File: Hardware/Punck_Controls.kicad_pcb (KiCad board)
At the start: 2 copper layers, 91.2 x 110 mm, 37 parts, among them J1 Conn_01x12_Female, J10 Kick_In, J11 USB_B_Micro, J12 Tempo_Out, J13 Audio_Out_L, J14 Audio_Out_R, J15 Midi_In, J2 Conn_01x12_Female, J3 Conn_01x12_Female, J4 Conn_01x12_Female, J5 Snare_In, J6 CH_In, J7 OH_In, J8 SamplerA_In, J9 SamplerB_In

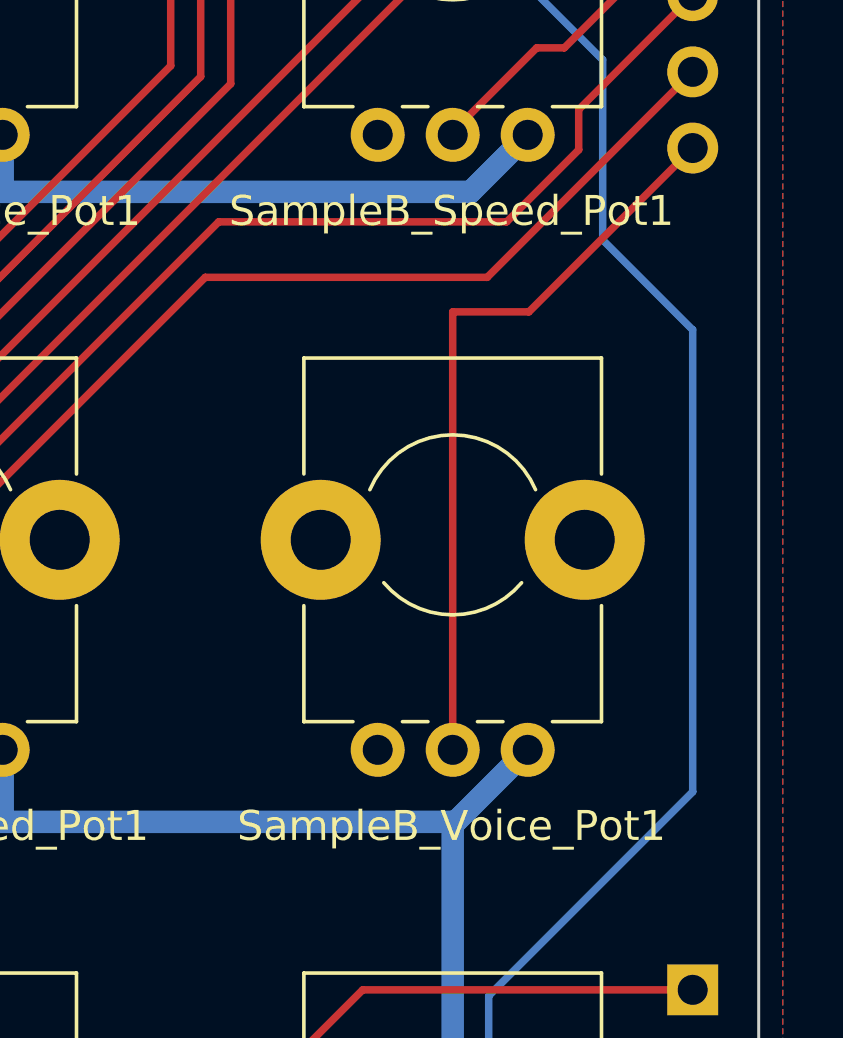
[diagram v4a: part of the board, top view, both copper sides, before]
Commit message: Updated components on panel board
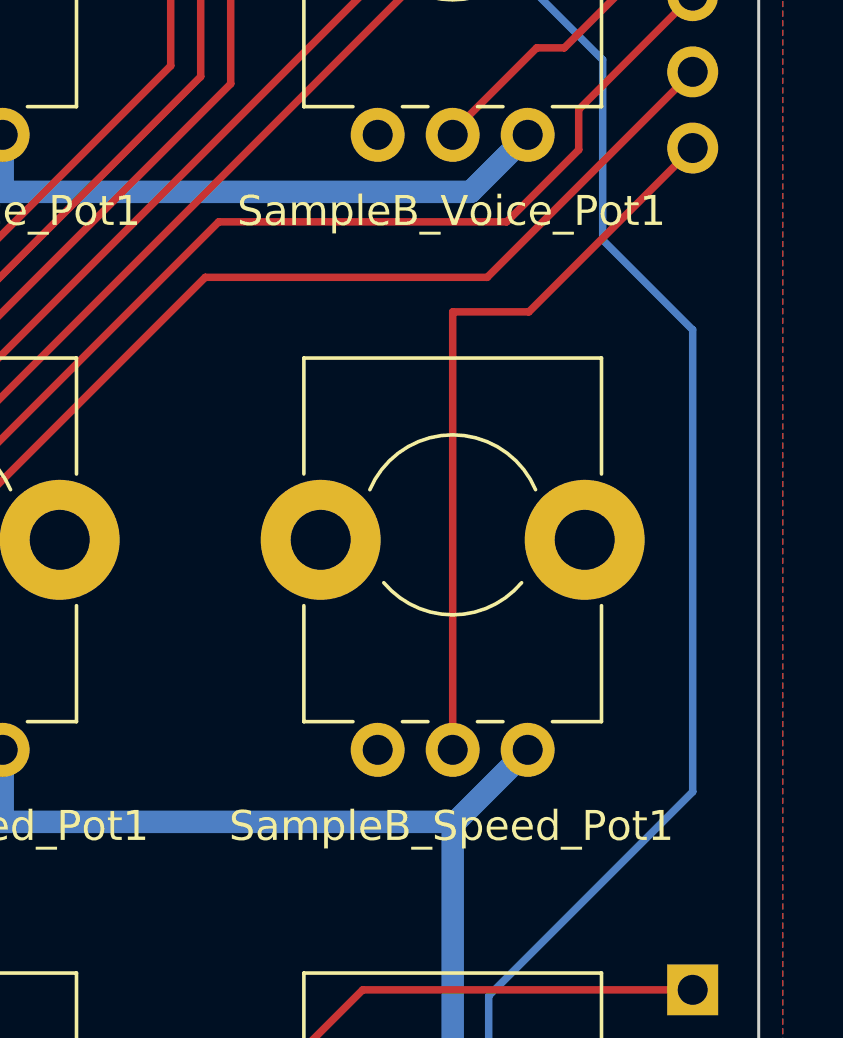
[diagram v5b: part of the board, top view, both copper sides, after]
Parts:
- moved SampleB_Speed_Pot1 20.5 mm to (151.0, 96.5)
- moved SampleB_Voice_Pot1 20.5 mm to (151.0, 76.0)
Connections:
- J1 pad 12: /SAMPLER_B_VOICE_POT -> /SAMPLER_B_SPEED_POT
- J1 pad 9: /SAMPLER_B_SPEED_POT -> /SAMPLER_B_VOICE_POT
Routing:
- net /SAMPLER_B_VOICE_POT: track 24.9 -> 11.0 mm
- net /SAMPLER_B_SPEED_POT: track 11.0 -> 24.9 mm
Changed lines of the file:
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@@
   )
   (footprint "Custom_Footprints:Alpha_9mm_Potentiometer_Aligned" (layer "F.Cu")
-    (at 151 76)
+    (at 151 96.5)
     (descr "Potentiometer 9mm")
     (tags "Potentiometer 9mm")
@@
   )
   (footprint "Custom_Footprints:Alpha_9mm_Potentiometer_Aligned" (layer "F.Cu")
-    (at 151 96.5)
+    (at 151 76)
     (descr "Potentiometer 9mm")
     (tags "Potentiometer 9mm")
@@
       (net 13 "/HIHAT_DECAY_POT") (pinfunction "Pin_8") (pintype "passive"))
     (pad "9" thru_hole oval (at 0 -20.32 180) (size 1.7 1.7) (drill 1) (layers *.Cu *.Mask)
-      (net 30 "/SAMPLER_B_SPEED_POT") (pinfunction "Pin_9") (pintype "passive"))
+      (net 26 "/SAMPLER_B_VOICE_POT") (pinfunction "Pin_9") (pintype "passive"))
     (pad "10" thru_hole oval (at 0 -22.86 180) (size 1.7 1.7) (drill 1) (layers *.Cu *.Mask)
       (net 32 "/SNARE_VOL_POT") (pinfunction "Pin_10") (pintype "passive"))
@@
       (net 29 "/SAMPLER_A_SPEED_POT") (pinfunction "Pin_11") (pintype "passive"))
     (pad "12" thru_hole oval (at 0 -27.94 180) (size 1.7 1.7) (drill 1) (layers *.Cu *.Mask)
-      (net 26 "/SAMPLER_B_VOICE_POT") (pinfunction "Pin_12") (pintype "passive"))
+      (net 30 "/SAMPLER_B_SPEED_POT") (pinfunction "Pin_12") (pintype "passive"))
     (model "${KICAD6_3DMODEL_DIR}/Connector_PinHeader_2.54mm.3dshapes/PinHeader_1x12_P2.54mm_Vertical.wrl"
       (offset (xyz 0 0 0))
@@
   (segment (start 141.7 63.6) (end 133.5 71.8) (width 0.25) (layer "F.Cu") (net 25))
   (segment (start 158.12 61.08) (end 155.6 63.6) (width 0.25) (layer "F.Cu") (net 25))
-  (segment (start 153.54 89.4) (end 159 83.94) (width 0.25) (layer "F.Cu") (net 26))
-  (segment (start 151 104) (end 151 89.4) (width 0.25) (layer "F.Cu") (net 26))
-  (segment (start 151 89.4) (end 153.54 89.4) (width 0.25) (layer "F.Cu") (net 26))
+  (segment (start 153.8 80.6) (end 154.72 80.6) (width 0.25) (layer "F.Cu") (net 26))
+  (segment (start 151 83.5) (end 151 83.4) (width 0.25) (layer "F.Cu") (net 26))
+  (segment (start 154.72 80.6) (end 159 76.32) (width 0.25) (layer "F.Cu") (net 26))
+  (segment (start 151 83.4) (end 153.8 80.6) (width 0.25) (layer "F.Cu") (net 26))
   (segment (start 154.26 114.54) (end 146.6 122.2) (width 0.25) (layer "F.Cu") (net 27))
   (segment (start 146.6 122.2) (end 135.8 122.2) (width 0.25) (layer "F.Cu") (net 27))
@@
   (segment (start 152.150489 88.249511) (end 159 81.4) (width 0.25) (layer "F.Cu") (net 29))
   (segment (start 133.5 97.5) (end 142.750489 88.249511) (width 0.25) (layer "F.Cu") (net 29))
-  (segment (start 153.8 80.6) (end 154.72 80.6) (width 0.25) (layer "F.Cu") (net 30))
-  (segment (start 151 83.5) (end 151 83.4) (width 0.25) (layer "F.Cu") (net 30))
-  (segment (start 154.72 80.6) (end 159 76.32) (width 0.25) (layer "F.Cu") (net 30))
-  (segment (start 151 83.4) (end 153.8 80.6) (width 0.25) (layer "F.Cu") (net 30))
+  (segment (start 153.54 89.4) (end 159 83.94) (width 0.25) (layer "F.Cu") (net 30))
+  (segment (start 151 104) (end 151 89.4) (width 0.25) (layer "F.Cu") (net 30))
+  (segment (start 151 89.4) (end 153.54 89.4) (width 0.25) (layer "F.Cu") (net 30))
   (segment (start 159 58.54) (end 154.74 62.8) (width 0.25) (layer "F.Cu") (net 31))
   (segment (start 119.6 81.4) (end 100.6 81.4) (width 0.25) (layer "F.Cu") (net 31))

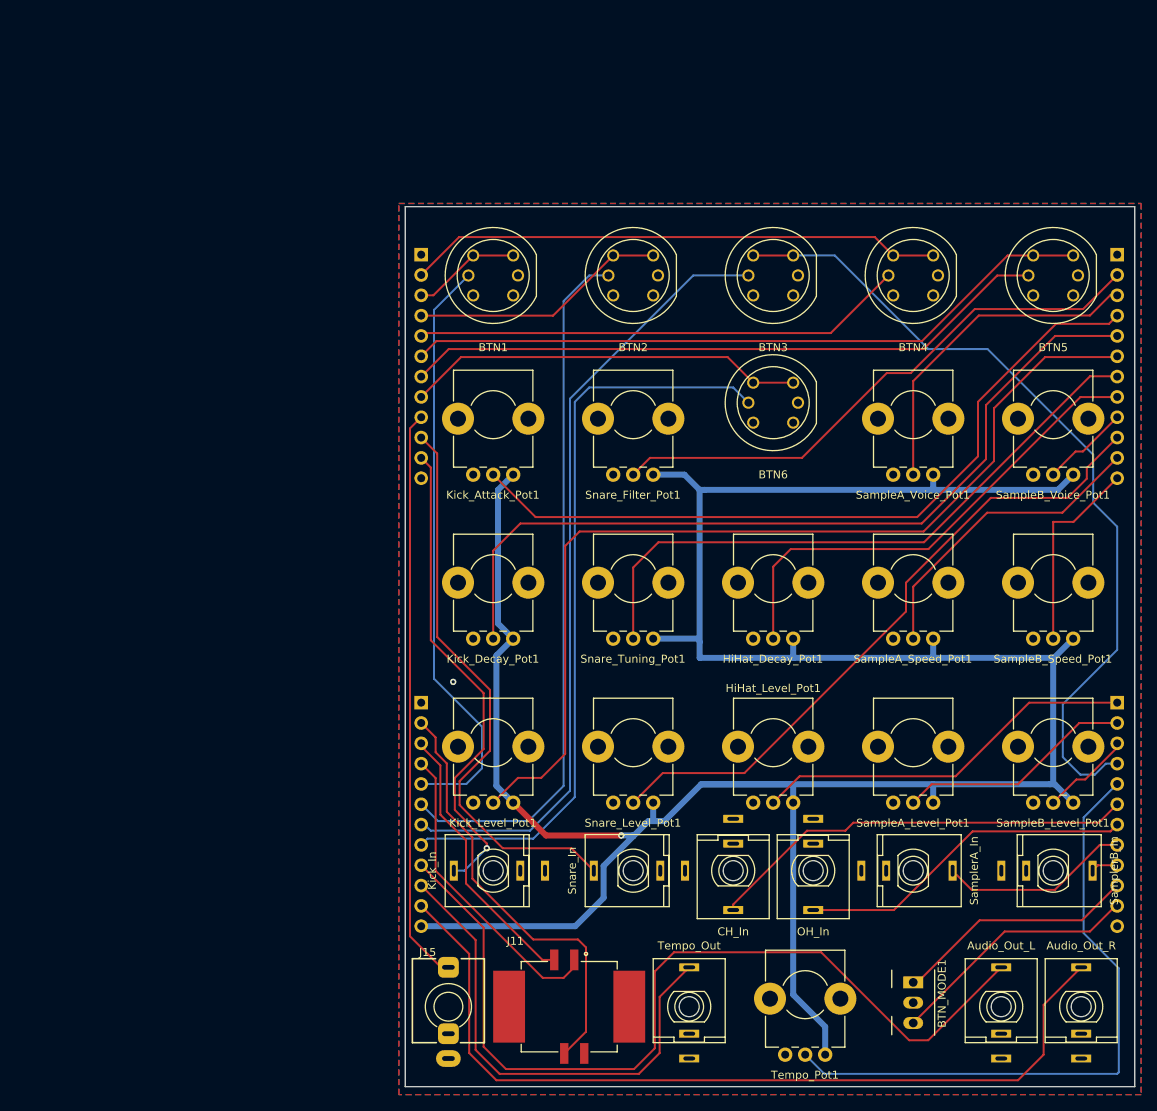
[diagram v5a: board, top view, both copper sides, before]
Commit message: Updated PCBs to match changes in panel; ground returns improved
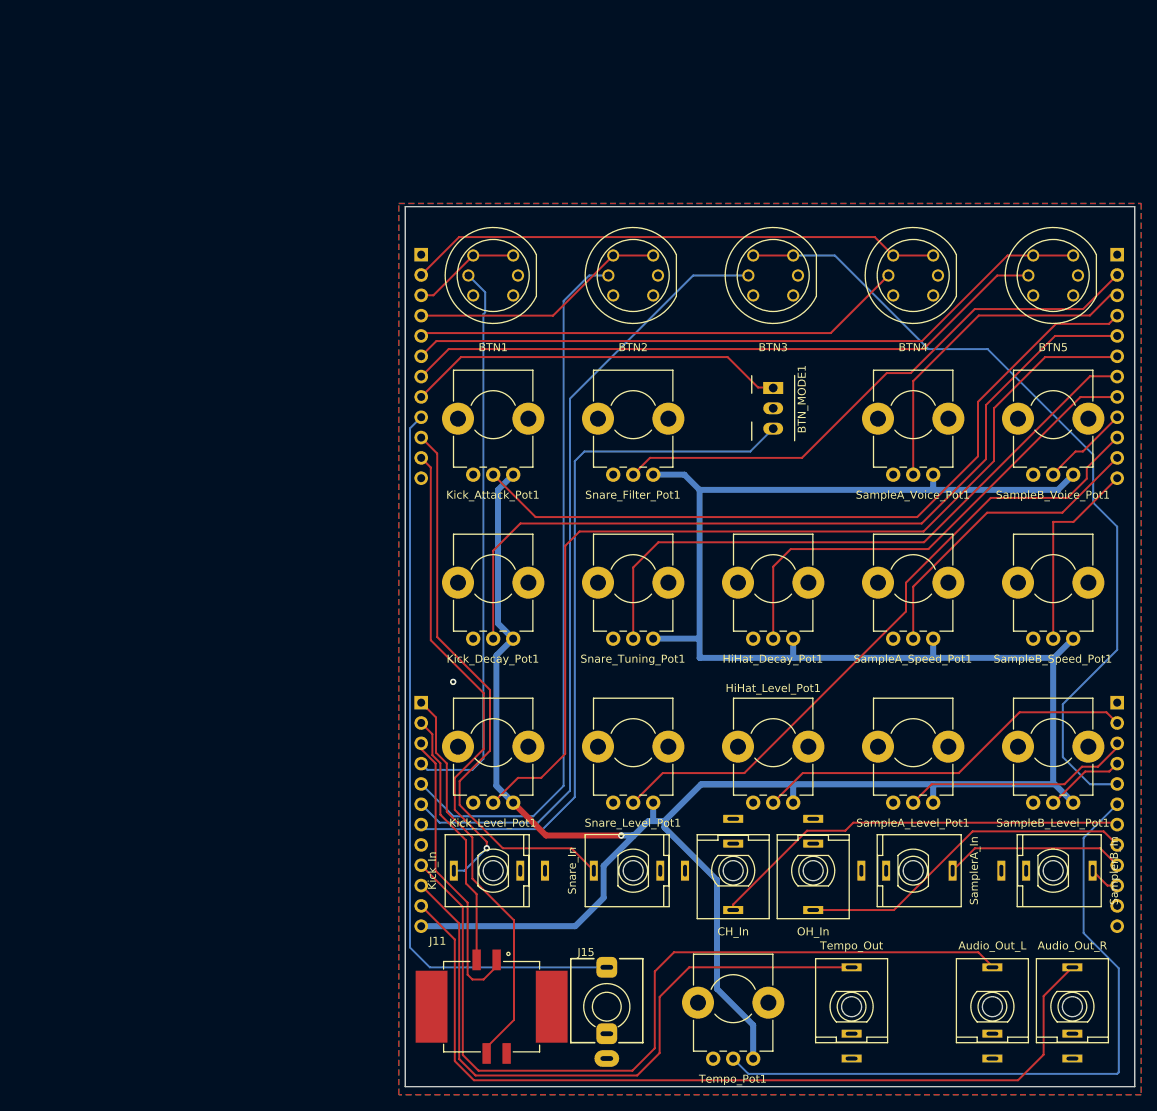
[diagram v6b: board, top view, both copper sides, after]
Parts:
- removed BTN6: KS01-BLV, Custom_Footprints:KS01-BLV
- moved BTN_MODE1 76.3 mm to (116.0, 75.2)
- moved J12 20.3 mm to (125.8, 150.0)
- moved J15 19.8 mm to (95.2, 150.0)
- moved J11 9.70 mm to (80.8, 150.0)
- moved Tempo_Pot1 9.01 mm to (111.0, 149.0)
- moved J13 1.10 mm to (143.4, 150.0)
- moved J14 1.10 mm to (153.4, 150.0)
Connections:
- BTN3 pad 1: /CH_BTN -> /HH_BTN
- BTN3 pad 2: /CH_BTN -> /HH_BTN
- BTN3 pad 5: /CH_LED -> /HH_LED
- J2 pad 1: /HIHAT_VOL_POT -> GND
- J2 pad 10: /MIDI_LEARN -> /SAMPLER_B_IN
- J2 pad 11: /SEQ_SELECT -> unconnected-(J2-Pad11)
- J2 pad 2: /SAMPLER_A_VOL_POT -> /HIHAT_VOL_POT
- J2 pad 3: /SAMPLER_B_VOL_POT -> /SAMPLER_A_VOL_POT
- J2 pad 4: /CH_BTN -> /SAMPLER_B_VOL_POT
- J2 pad 5: /TEMPO_POT -> /HH_BTN
- J2 pad 6: /CH_IN -> /TEMPO_POT
- J2 pad 7: /OH_IN -> /CH_IN
- J2 pad 8: /SAMPLER_A_IN -> /OH_IN
- J2 pad 9: /SAMPLER_B_IN -> /SAMPLER_A_IN
- J3 pad 8: /OH_BTN -> /MIDI_LEARN
- J4 pad 1: GND -> /USB_DP
- J4 pad 2: /USB_DP -> /USB_DM
- J4 pad 3: /USB_DM -> /USB_VBUS
- J4 pad 4: /USB_VBUS -> /KI_LED
- J4 pad 5: /KI_LED -> /SN_LED
- J4 pad 6: /SN_LED -> /HH_LED
- J4 pad 7: /CH_LED -> /SEQ_SELECT
- J4 pad 8: /OH_LED -> GND
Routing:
- net /CH_BTN: track 103.0 -> 0.00 mm
- net /HH_BTN: track 0.00 -> 102.9 mm
- net /HH_LED: track 0.00 -> 98.9 mm
- net /CH_LED: track 98.7 -> 0.00 mm
- net /OH_LED: track 94.3 -> 0.00 mm
- net /SEQ_SELECT: track 31.6 -> 89.6 mm
- net /OH_BTN: track 49.9 -> 0.00 mm
- net /TEMPO_OUT: track 60.9 -> 83.3 mm
- net /MIDI_IN: track 71.9 -> 92.5 mm
- net /MIDI_LEARN: track 30.5 -> 47.7 mm
- net /TEMPO_POT: track 79.9 -> 86.1 mm
- net /AUDIO_OUT_L: track 111.8 -> 105.5 mm
- net /KI_LED: track 74.3 -> 70.1 mm
- net /USB_DP: track 54.2 -> 50.1 mm
- net /USB_DM: track 34.8 -> 32.5 mm
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
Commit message: More PCB tweaking
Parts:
- moved J11 0.40 mm to (80.4, 150.0)
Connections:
- J2 pad 11: unconnected-(J2-Pad11) -> /TEMPO_OUT
- J4 pad 10: /TEMPO_OUT -> /AUDIO_OUT_L
- J4 pad 9: /AUDIO_OUT_L -> GND
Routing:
- net /TEMPO_OUT: track 83.3 -> 36.4 mm
- net /AUDIO_OUT_L: track 105.5 -> 97.2 mm
- net GND: vias 1 -> 6

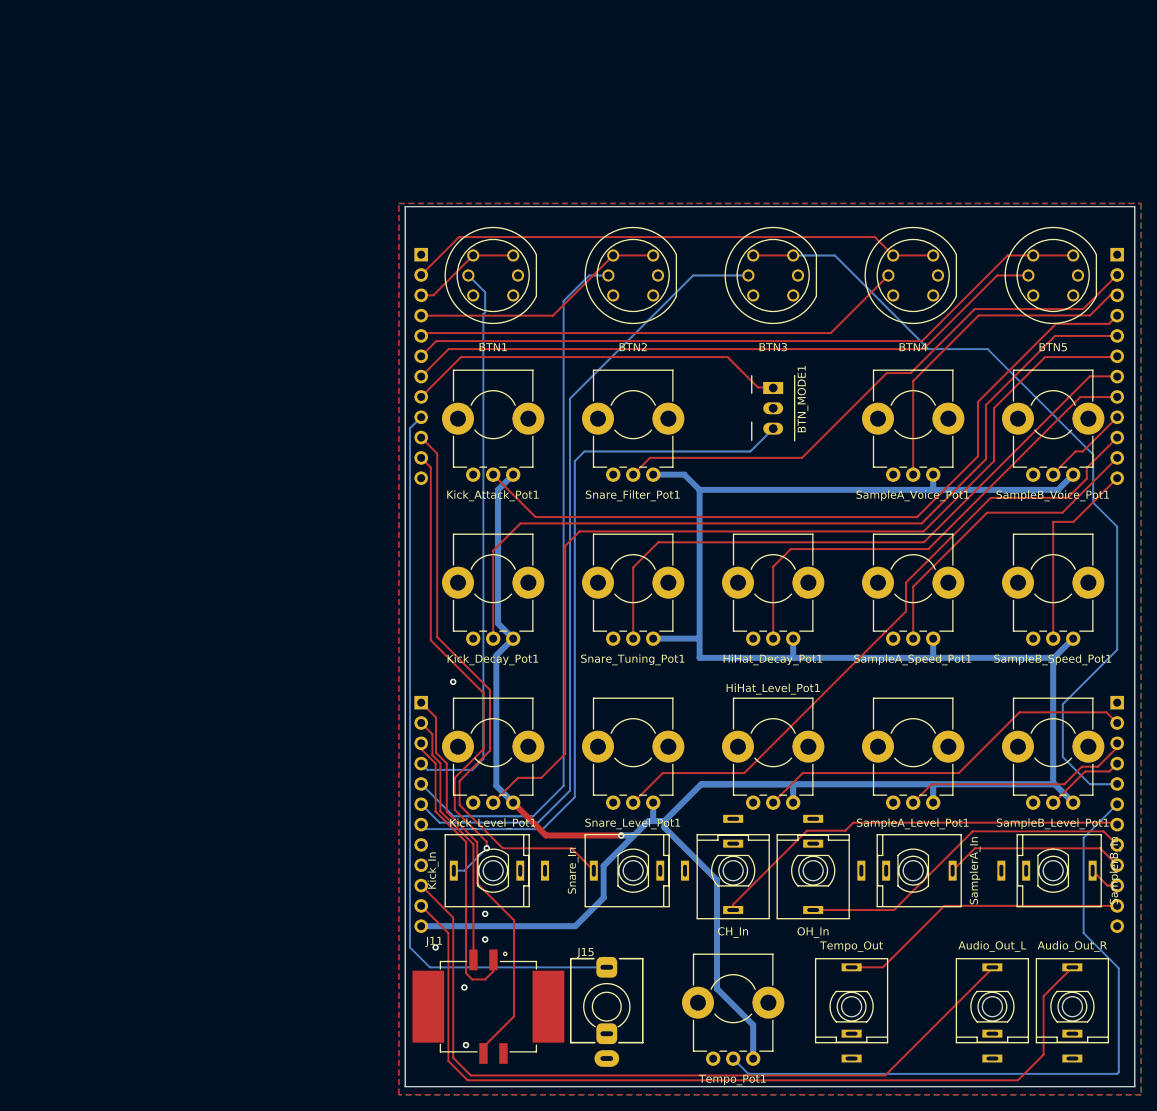
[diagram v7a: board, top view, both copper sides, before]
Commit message: More PCB tweaks; rejigged bottom row of controls
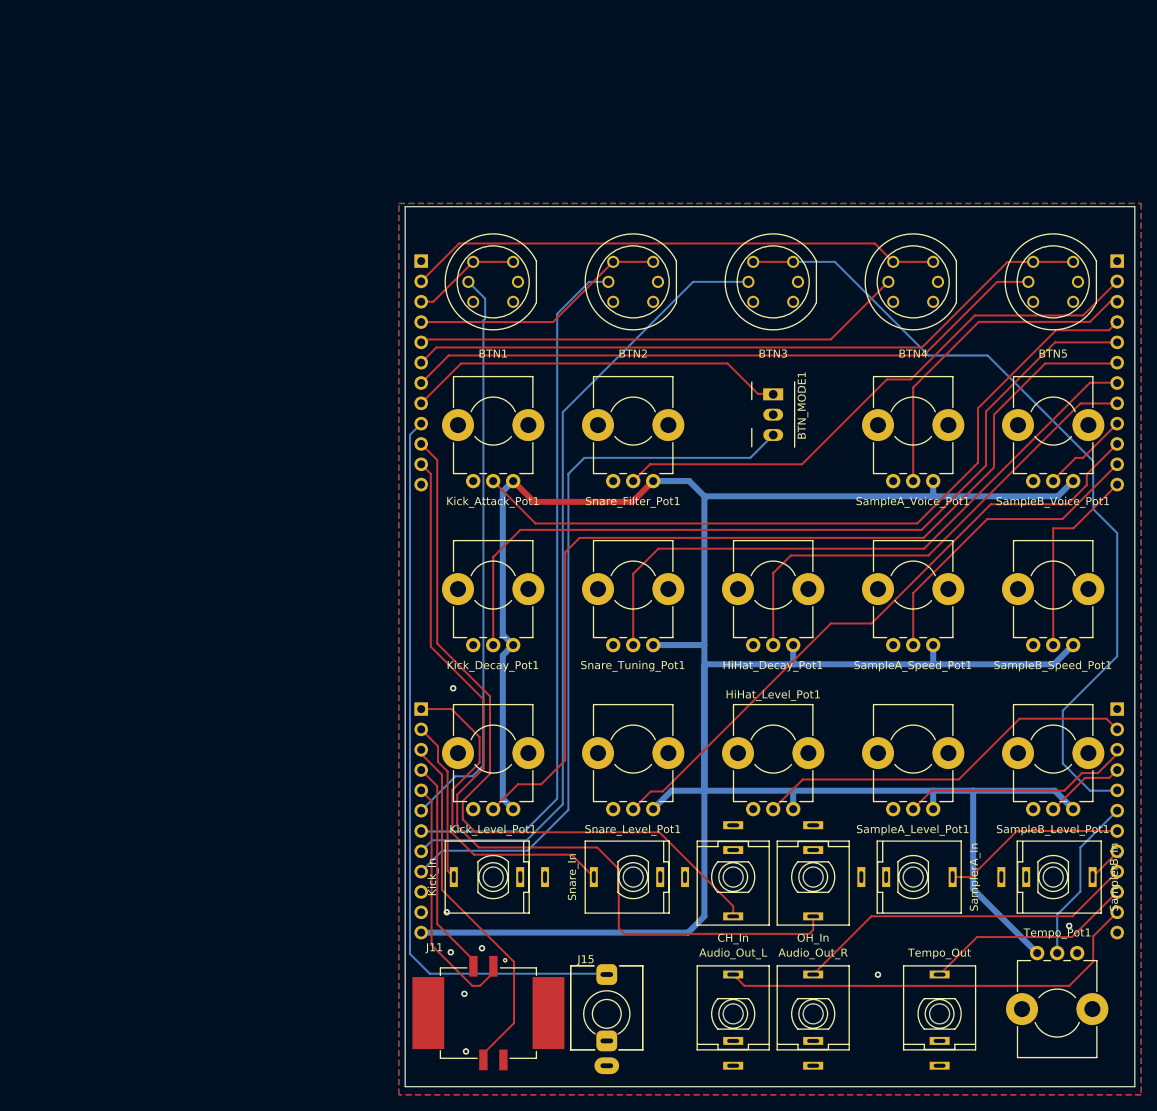
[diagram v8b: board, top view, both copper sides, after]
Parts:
- moved Tempo_Pot1 40.5 mm to (151.5, 150.8), turned to 180 degrees
- moved J13 32.4 mm to (111.0, 150.9)
- moved J14 32.4 mm to (121.0, 150.9)
- moved J12 11.0 mm to (136.8, 150.9)
- moved J15 0.90 mm to (95.2, 150.9)
- moved J10 0.80 mm to (81.0, 133.8)
- moved J11 0.80 mm to (80.4, 150.8)
- moved J5 0.80 mm to (98.5, 133.8)
- moved J6 0.80 mm to (111.0, 133.8)
- moved J7 0.80 mm to (121.0, 133.8)
- moved J8 0.80 mm to (133.5, 133.8)
- moved J9 0.80 mm to (151.0, 133.8)
- moved BTN1 0.80 mm to (81.0, 59.4)
- moved BTN2 0.80 mm to (98.5, 59.4)
- moved BTN3 0.80 mm to (116.0, 59.4)
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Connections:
- J2 pad 10: /SAMPLER_B_IN -> /TEMPO_OUT
- J2 pad 11: /TEMPO_OUT -> /AUDIO_OUT_L
- J2 pad 7: /CH_IN -> /SAMPLER_A_IN
- J2 pad 8: /OH_IN -> /SAMPLER_B_IN
- J2 pad 9: /SAMPLER_A_IN -> /AUDIO_OUT_R
- J3 pad 10: /SNARE_IN -> /CH_IN
- J3 pad 11: /KICK_IN -> /OH_IN
- J4 pad 1: /USB_DP -> /SNARE_IN
- J4 pad 10: /AUDIO_OUT_L -> GND
- J4 pad 11: /AUDIO_OUT_R -> GND
- J4 pad 2: /USB_DM -> /KICK_IN
- J4 pad 3: /USB_VBUS -> /USB_DP
- J4 pad 4: /KI_LED -> /USB_DM
- J4 pad 5: /SN_LED -> /USB_VBUS
- J4 pad 6: /HH_LED -> /KI_LED
- J4 pad 7: /SEQ_SELECT -> /SN_LED
- J4 pad 8: GND -> /HH_LED
- J4 pad 9: GND -> /SEQ_SELECT
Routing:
- net /AUDIO_OUT_R: track 109.9 -> 43.3 mm
- net /TEMPO_POT: track 86.1 -> 20.9 mm
- net /OH_IN: track 42.8 -> 106.1 mm
- net /AUDIO_OUT_L: track 97.2 -> 54.3 mm
- net /KICK_IN: track 60.5 -> 20.1 mm, vias 1 -> 0
- net /CH_IN: track 53.0 -> 91.5 mm
- net /SNARE_IN: track 71.3 -> 42.1 mm
- net /TEMPO_OUT: track 36.4 -> 26.5 mm
- net +3.3VA: track 356.6 -> 364.2 mm, vias 1 -> 0
- net /USB_VBUS: track 36.6 -> 31.1 mm
- net /USB_DM: track 32.3 -> 27.2 mm
- net /USB_DP: track 50.2 -> 45.9 mm
- net /SNARE_VOL_POT: track 82.3 -> 80.2 mm
- net /SEQ_SELECT: track 89.6 -> 91.2 mm
- net /KI_LED: track 70.1 -> 71.5 mm
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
